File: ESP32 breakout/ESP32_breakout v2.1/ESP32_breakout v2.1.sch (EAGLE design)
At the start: 49 parts, among them J2 JUMPER_2-WAY, Q1 BSS84, Q2 BSS84, Q3 BSS84, U1 ESP-WROOM-32, U2 NCP-1117, Y1 12MHz

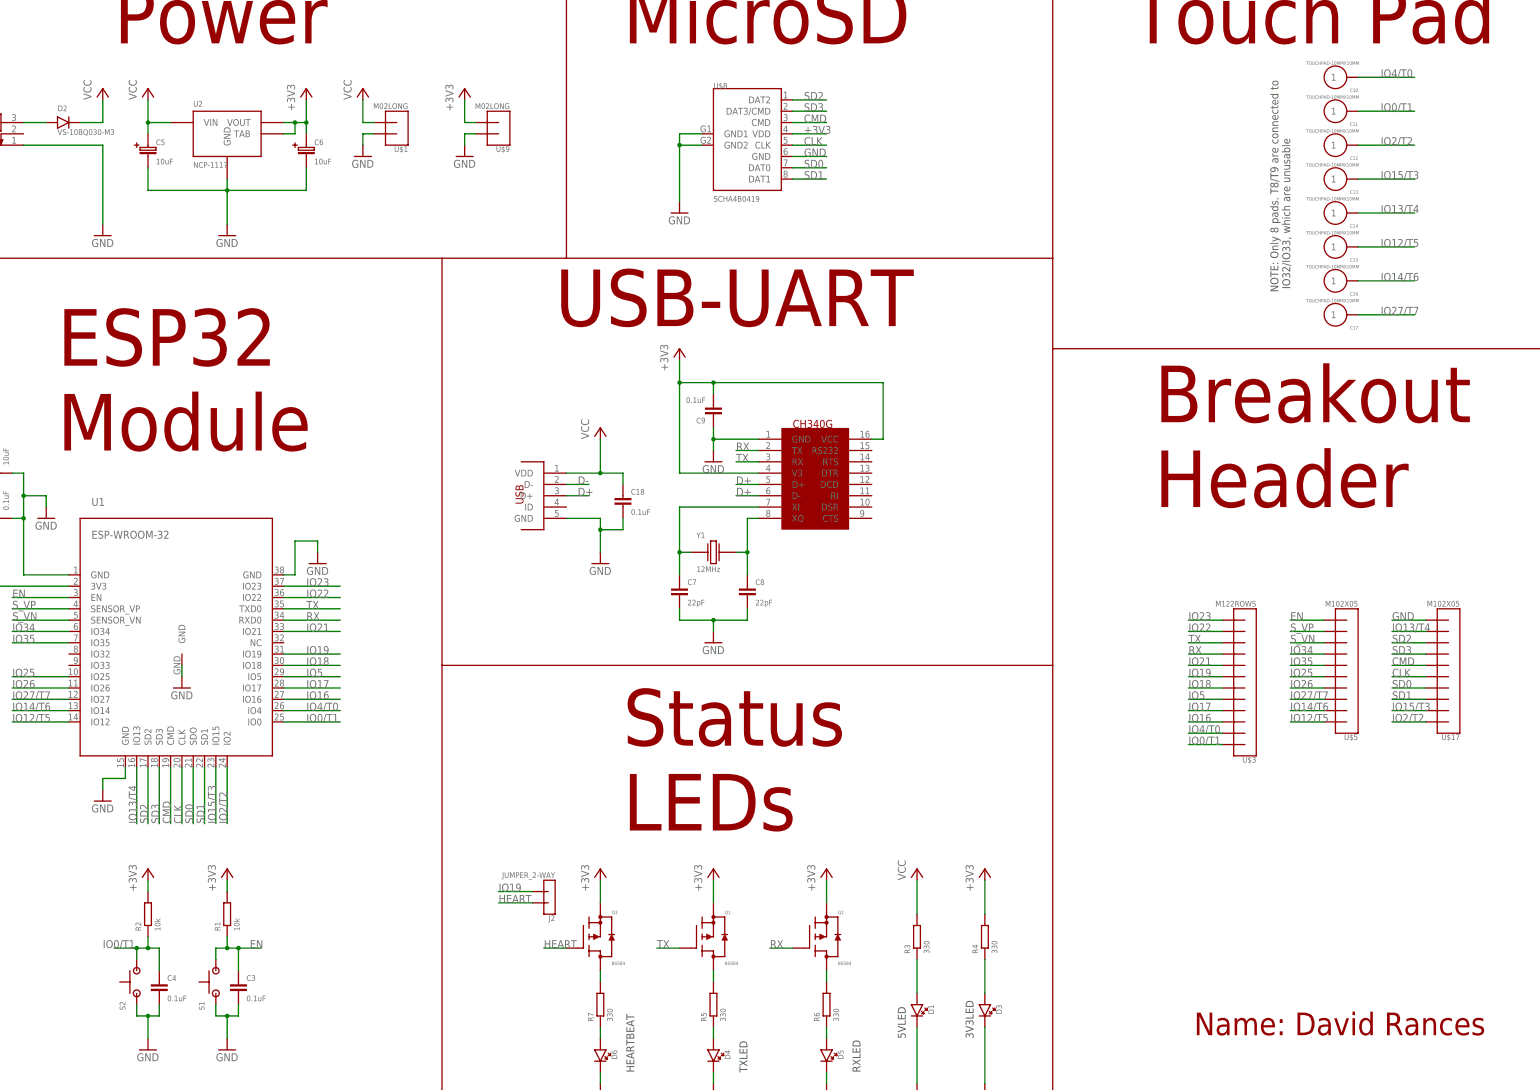
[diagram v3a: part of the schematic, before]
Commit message: Modified labels
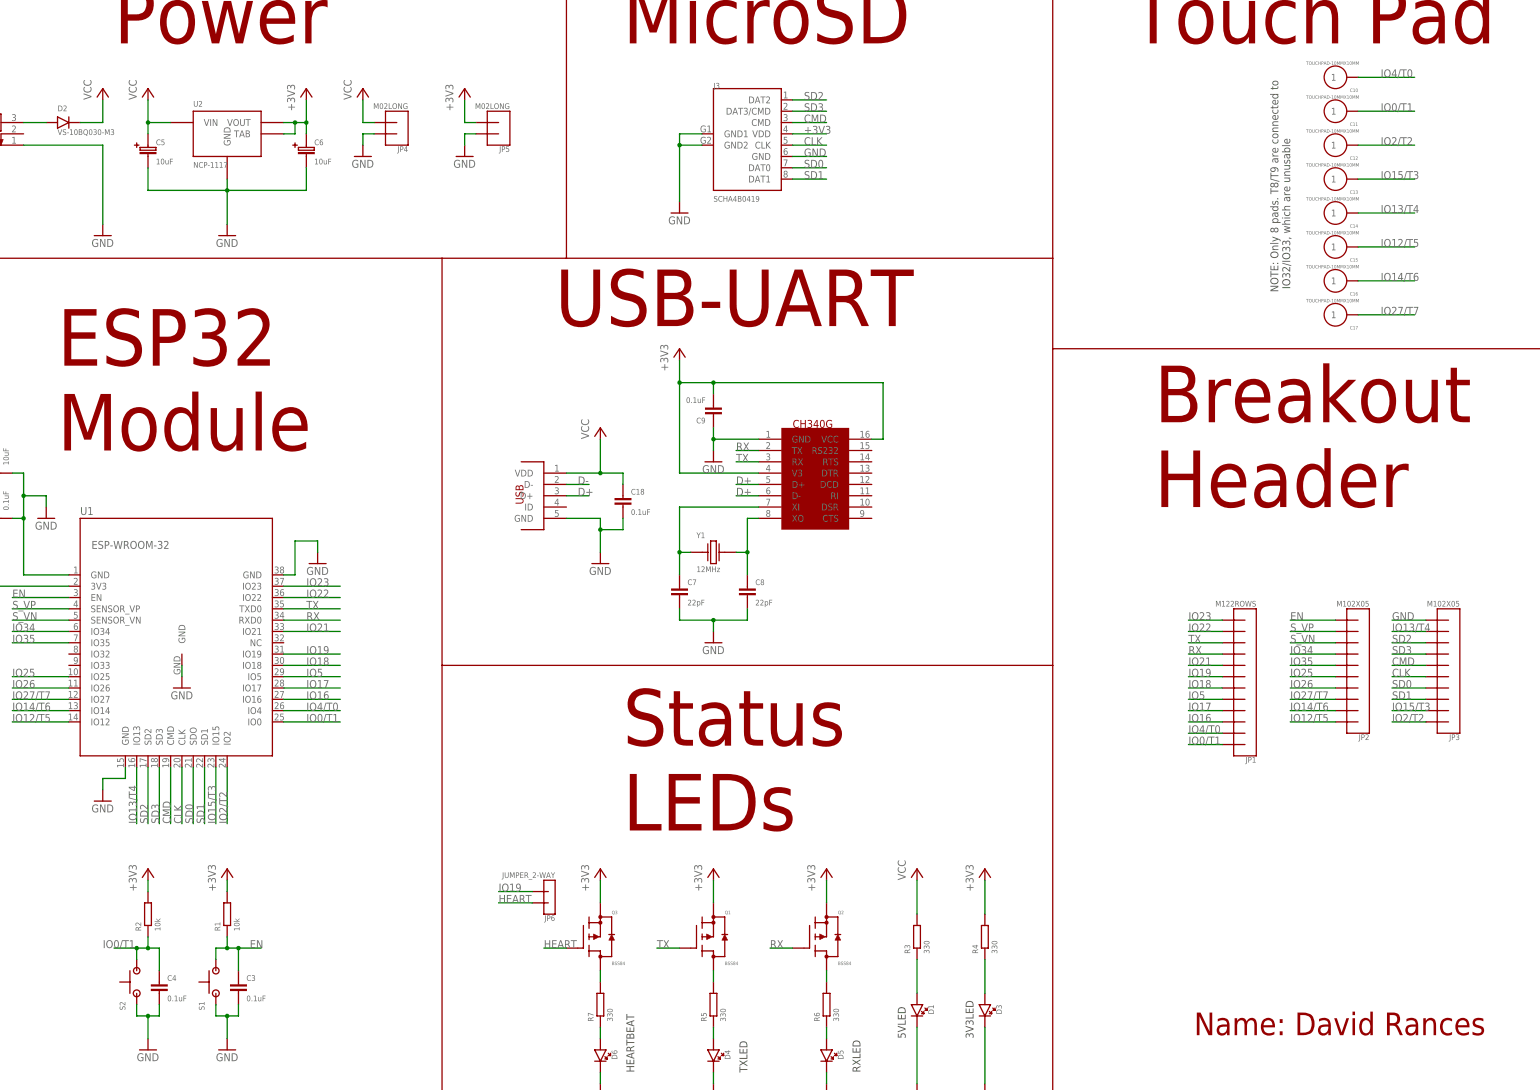
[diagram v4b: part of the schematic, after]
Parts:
- removed U$5: M102X05, dr-library:M102X05
- added JP2: M102X05, dr-library:M102X05
- renumbered J2 to JP6, U$1 to JP4, U$17 to JP3, U$3 to JP1, U$8 to J3, U$9 to JP5
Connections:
- net EN: now also JP2.10; no longer U$5.10
- net IO12/T5: now also JP2.1; no longer U$5.1
- net IO14/T6: now also JP2.2; no longer U$5.2
- net IO25: now also JP2.5; no longer U$5.5
- net IO26: now also JP2.4; no longer U$5.4
- net IO27/T7: now also JP2.3; no longer U$5.3
- net IO34: now also JP2.7; no longer U$5.7
- net IO35: now also JP2.6; no longer U$5.6
- net S_VN: now also JP2.8; no longer U$5.8
- net S_VP: now also JP2.9; no longer U$5.9

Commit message: DRU check
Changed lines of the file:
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@@
 <pinref part="U$7" gate="G$1" pin="D-"/>
 <wire x1="190.5" y1="147.32" x2="185.42" y2="147.32" width="0.1524" layer="91"/>
+<label x="185.42" y="147.32" size="1.778" layer="95"/>
 </segment>
 </net>
@@
 <wire x1="190.5" y1="149.86" x2="185.42" y2="149.86" width="0.1524" layer="91"/>
 <label x="185.42" y="149.86" size="1.778" layer="95"/>
-<label x="185.42" y="147.32" size="1.778" layer="95"/>
 </segment>
 </net>
@@
 </sheet>
 </sheets>
-<errors>
-</errors>
 </schematic>
 </drawing>
